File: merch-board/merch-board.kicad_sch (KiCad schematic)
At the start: 16 parts, among them P1 USB_C_Plug, SW3 OCT_DOWN, SW4 OCT_UP, SW5 TONE_SEL, U1 NCP1117-3.3_SOT223

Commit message: Add LCSC part numbers
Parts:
- C1, C2: LCSC (none) -> C15850
- D1, D2, D3, D4: LCSC (none) -> C2286
- R24, R25, R26, R31: LCSC (none) -> C25076
- SW3, SW4, SW5: LCSC (none) -> C2888740
- U1: LCSC (none) -> C26537
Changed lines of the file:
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@@
+			)
+		)
+		(property "LCSC" "C26537"
+			(at 41.91 125.73 0)
+			(effects
+				(font
+					(size 1.27 1.27)
+				)
+				(hide yes)
 			)
 		)
@@
 			)
 		)
+		(property "LCSC" "C15850"
+			(at 24.13 130.81 0)
+			(effects
+				(font
+					(size 1.27 1.27)
+				)
+				(hide yes)
+			)
+		)
 		(pin "1"
 		)
@@
 					(size 1.27 1.27)
 				)
+			)
+		)
+		(property "LCSC" "C15850"
+			(at 59.69 130.81 0)
+			(effects
+				(font
+					(size 1.27 1.27)
+				)
+				(hide yes)
 			)
 		)
@@
 			)
 		)
+		(property "LCSC" "C25076"
+			(at 175.26 146.05 0)
+			(effects
+				(font
+					(size 1.27 1.27)
+				)
+				(hide yes)
+			)
+		)
 		(pin "1"
 		)
@@
 			)
 		)
+		(property "LCSC" "C2286"
+			(at 210.82 137.16 90)
+			(effects
+				(font
+					(size 1.27 1.27)
+				)
+				(hide yes)
+			)
+		)
 		(pin "1"
 		)
@@
 			)
 		)
+		(property "LCSC" "C2888740"
+			(at 104.14 107.95 90)
+			(effects
+				(font
+					(size 1.27 1.27)
+				)
+				(hide yes)
+			)
+		)
 		(pin "1"
 		)
@@
 			)
 		)
+		(property "LCSC" "C2888740"
+			(at 91.44 107.95 90)
+			(effects
+				(font
+					(size 1.27 1.27)
+				)
+				(hide yes)
+			)
+		)
 		(pin "1"
 		)
@@
 			)
 		)
+		(property "LCSC" "C2286"
+			(at 175.26 137.16 90)
+			(effects
+				(font
+					(size 1.27 1.27)
+				)
+				(hide yes)
+			)
+		)
 		(pin "1"
 		)
@@
 			)
 		)
+		(property "LCSC" "C2286"
+			(at 198.12 137.16 90)
+			(effects
+				(font
+					(size 1.27 1.27)
+				)
+				(hide yes)
+			)
+		)
 		(pin "1"
 		)
@@
 			)
 		)
+		(property "LCSC" "C25076"
+			(at 198.12 146.05 0)
+			(effects
+				(font
+					(size 1.27 1.27)
+				)
+				(hide yes)
+			)
+		)
 		(pin "1"
 		)
@@
 			)
 		)
+		(property "LCSC" "C25076"
+			(at 186.69 146.05 0)
+			(effects
+				(font
+					(size 1.27 1.27)
+				)
+				(hide yes)
+			)
+		)
 		(pin "1"
 		)
@@
 			)
 		)
+		(property "LCSC" "C2286"
+			(at 186.69 137.16 90)
+			(effects
+				(font
+					(size 1.27 1.27)
+				)
+				(hide yes)
+			)
+		)
 		(pin "1"
 		)
@@
 			)
 		)
+		(property "LCSC" "C25076"
+			(at 210.82 146.05 0)
+			(effects
+				(font
+					(size 1.27 1.27)
+				)
+				(hide yes)
+			)
+		)
 		(pin "1"
 		)
@@
 			(effects
 				(font
+					(size 1.27 1.27)
+				)
+				(hide yes)
+			)
+		)
+		(property "LCSC" "C2888740"
+			(at 76.2 107.95 90)
+			(effects
+				(font

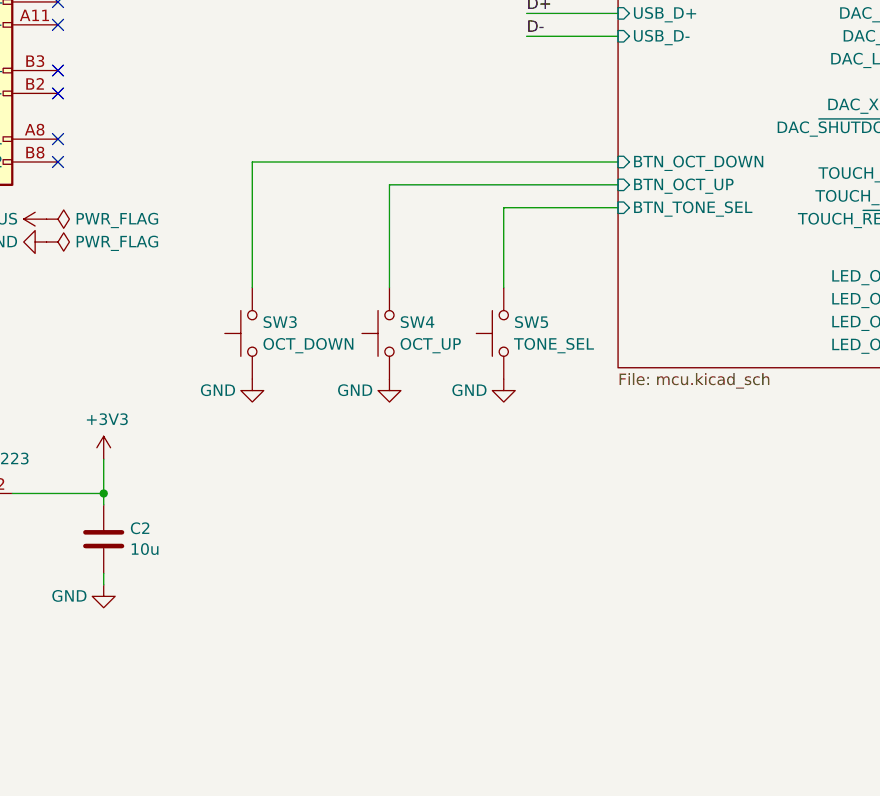
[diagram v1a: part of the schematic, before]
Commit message: Add volume pot to schematic
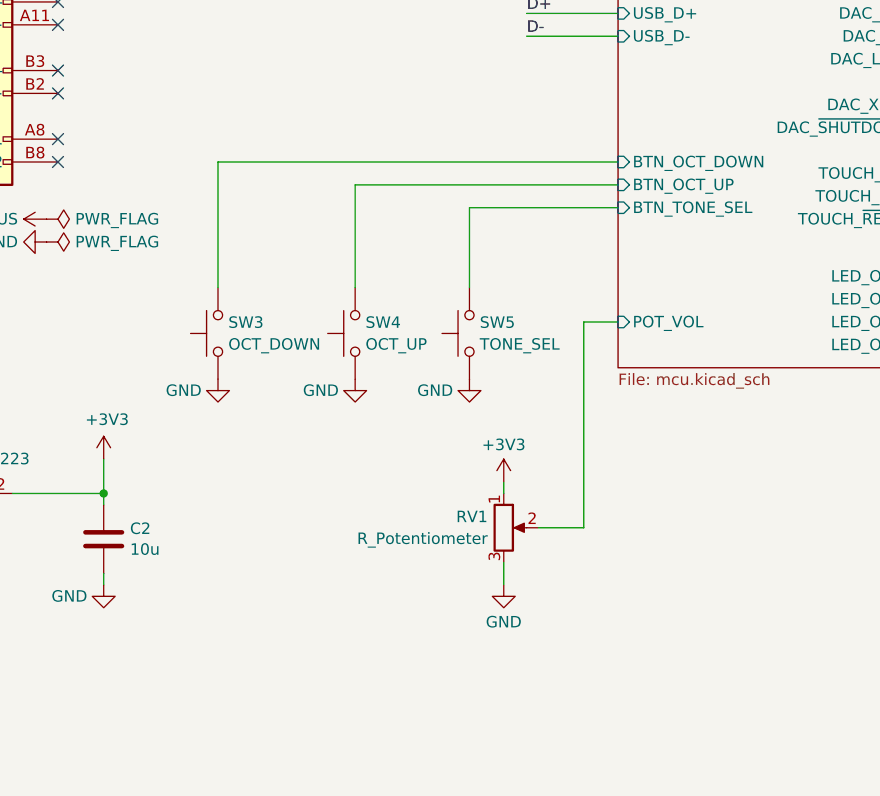
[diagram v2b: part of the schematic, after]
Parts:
- added RV1: R_Potentiometer, artsfest-touch:Potentiometer_SMD_Alps_RK10J1xR, symbol Device:R_Potentiometer
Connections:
- net +3V3: now also RV1.1
- net GND: now also RV1.3
- new net MCU/POT_VOL: RV1.2
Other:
- sheet MCU ports: added POT_VOL; removed none
- moved on the sheet: SW3, SW4, SW5

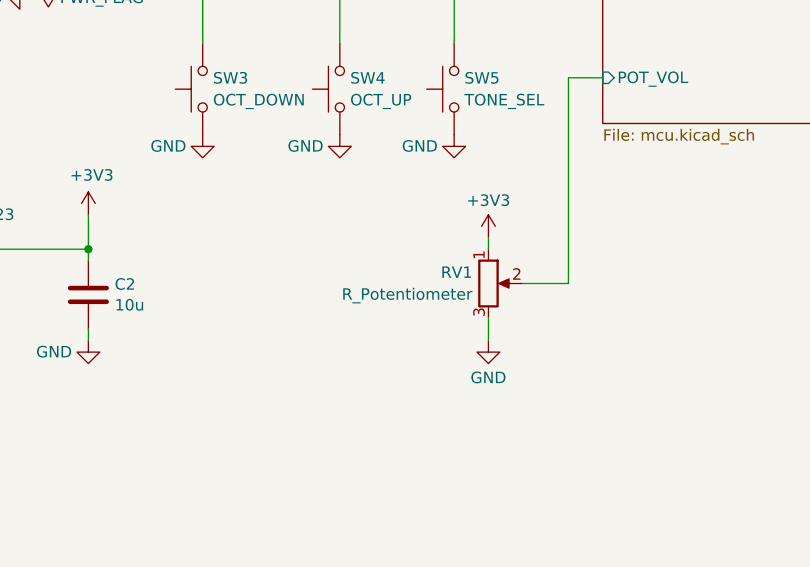
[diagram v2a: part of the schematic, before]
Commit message: Add volume pot to layout
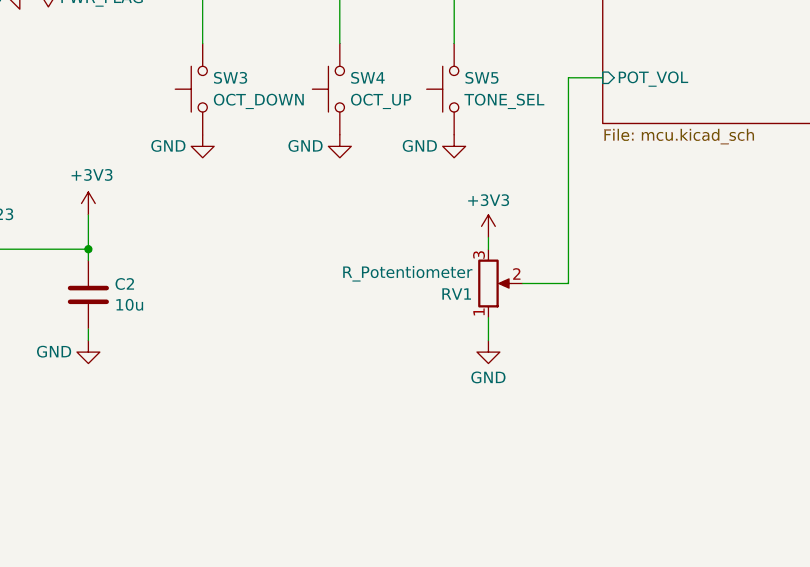
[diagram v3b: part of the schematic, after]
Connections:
- net +3V3: now also RV1.3; no longer RV1.1
- net GND: now also RV1.1; no longer RV1.3
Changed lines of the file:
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@@
 		(lib_id "Device:R_Potentiometer")
 		(at 104.14 129.54 0)
+		(mirror x)
 		(unit 1)
 		(exclude_from_sim no)
@@
 		(on_board yes)
 		(dnp no)
-		(fields_autoplaced yes)
 		(property "Reference" "RV1"
-			(at 102.362 128.3278 0)
+			(at 102.362 130.7522 0)
 			(effects
 				(font
@@
 		)
 		(property "Value" "R_Potentiometer"
-			(at 102.362 130.7521 0)
+			(at 102.362 128.3279 0)
 			(effects
 				(font

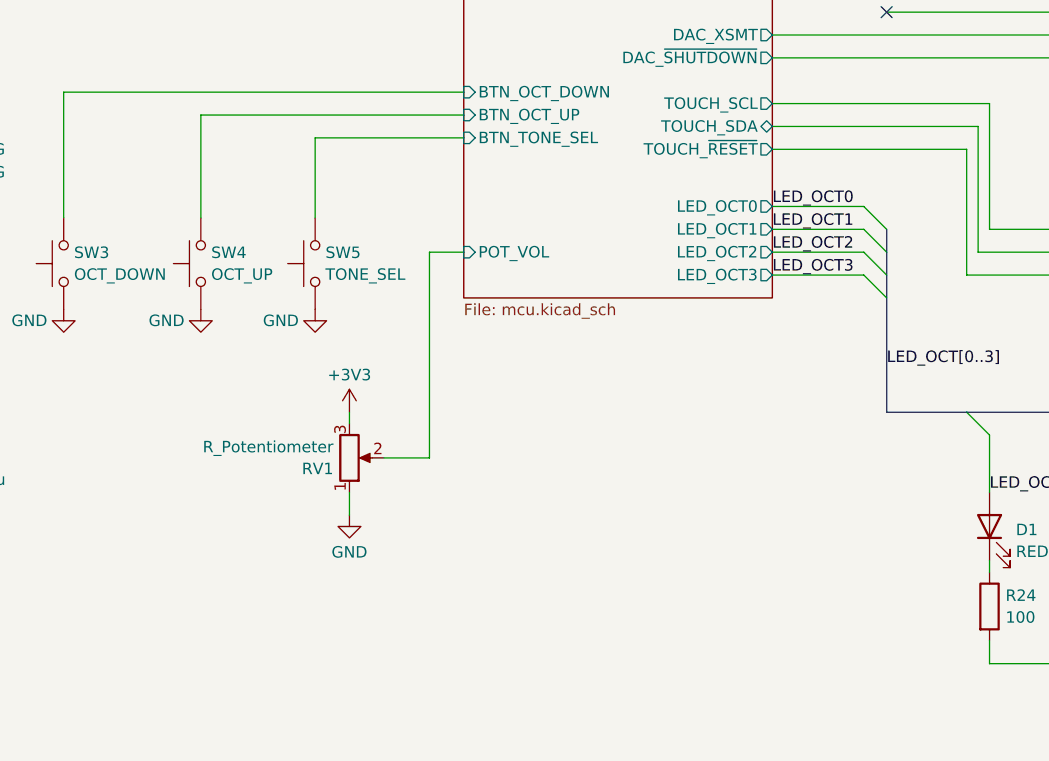
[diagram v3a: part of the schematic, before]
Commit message: Add WS2812B-2020 for tone indicator
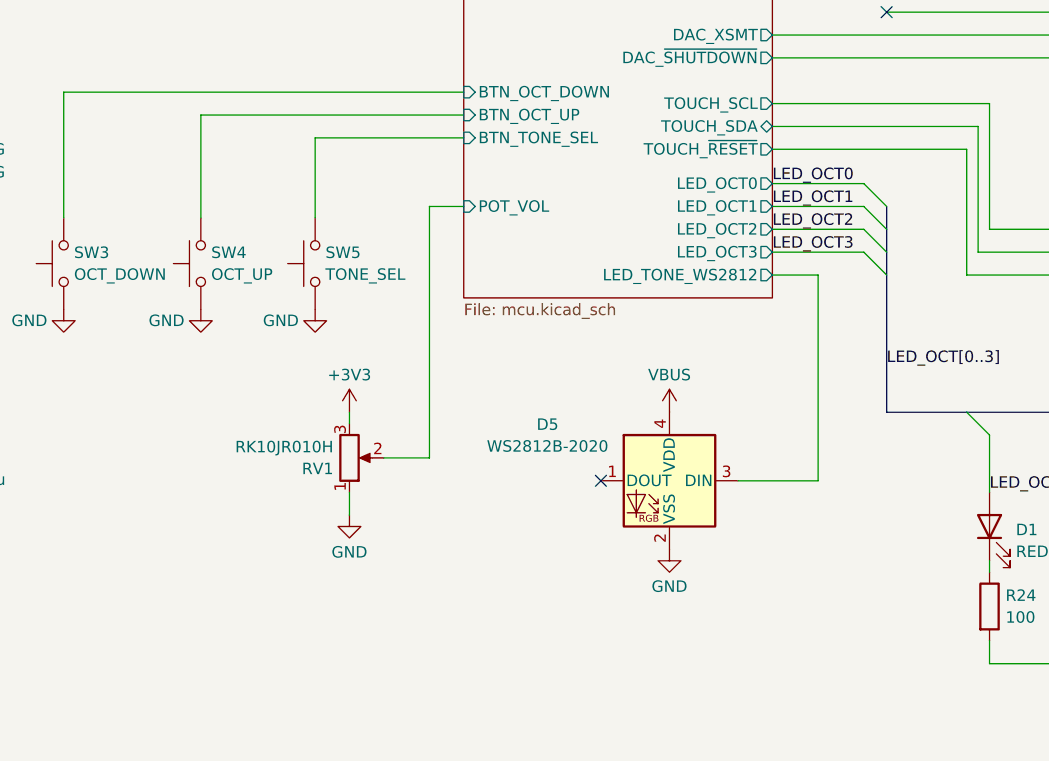
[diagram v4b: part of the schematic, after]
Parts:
- added D5: WS2812B-2020, LED_SMD:LED_WS2812B-2020_PLCC4_2.0x2.0mm, symbol LED:WS2812B-2020
- RV1: value R_Potentiometer -> RK10JR010H; LCSC (none) -> C470766
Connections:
- net GND: now also D5.2 (VSS)
- net VBUS: now also D5.4 (VDD)
- new net MCU/LED_TONE_WS2812: D5.3 (DIN)
- no-connect marks 12 -> 13
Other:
- sheet MCU ports: added LED_TONE_WS2812; removed none
